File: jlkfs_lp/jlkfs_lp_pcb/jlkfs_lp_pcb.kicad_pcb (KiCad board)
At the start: 2 copper layers, 158.1 x 125.8 mm, 40 parts, among them J0 USB_C_Receptacle_PowerOnly_6P, SW0 SWITCH, SW1 SWITCH, SW10 SWITCH, SW11 SWITCH, SW12 SWITCH, SW13 SWITCH, SW14 SWITCH, SW15 SWITCH, SW16 SWITCH, SW17 SWITCH, SW18 SWITCH, SW19 SWITCH, SW2 SWITCH, SW20 SWITCH, SW21 SWITCH, SW22 SWITCH, SW23 SWITCH, SW24 SWITCH, SW25 SWITCH, SW26 SWITCH, SW27 SWITCH, SW28 SWITCH, SW3 SWITCH, SW4 SWITCH, SW5 SWITCH, SW6 SWITCH, SW7 SWITCH, SW8 SWITCH, SW9 SWITCH, U0 RP2040

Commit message: Updates to jlkfs_lp.
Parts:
- removed H4, H5: MountingHole, MountingHole:MountingHole_3.5mm
- moved H1 134.4 mm to (95.0, 51.8)
- moved H2 117.2 mm to (142.5, 126.5)
- moved H0 68.9 mm to (171.0, 29.5)
- moved H3 54.2 mm to (228.0, 82.9)
- moved SW0 6.79 mm to (114.0, 51.8)
- moved SW12 6.79 mm to (95.0, 90.1)
- moved SW13 6.79 mm to (114.0, 87.8)
- moved SW19 6.79 mm to (95.0, 108.1)
- moved SW20 6.79 mm to (114.0, 105.8)
- moved SW5 6.79 mm to (95.0, 72.1)
- moved SW6 6.79 mm to (114.0, 69.8)
- moved J0 6.79 mm to (190.0, 20.0)
- moved R0 6.79 mm to (206.0, 34.0)
- moved R1 6.79 mm to (205.9, 36.5)
- moved SW1 6.79 mm to (133.0, 42.9)
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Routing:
- net GND: vias 0 -> 6
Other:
- board size 158.1 x 125.8 mm -> 157.5 x 125.8 mm

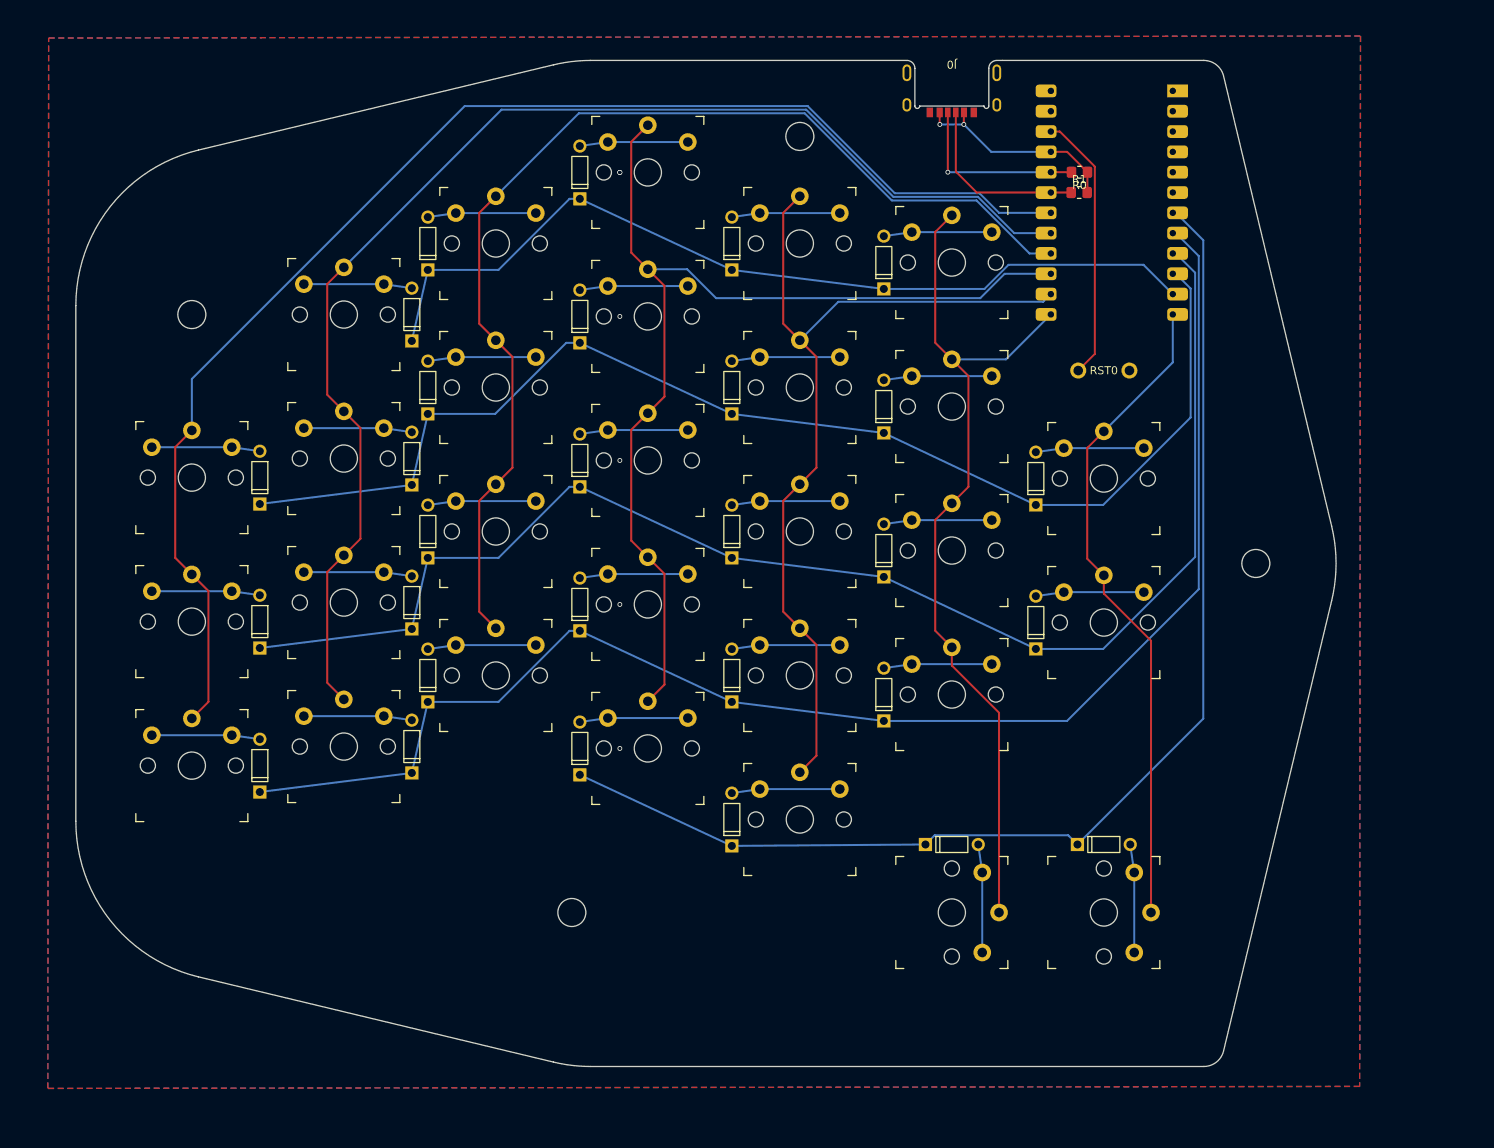
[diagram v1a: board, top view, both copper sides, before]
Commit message: Added a battery path for nice!nano to jlkfs.
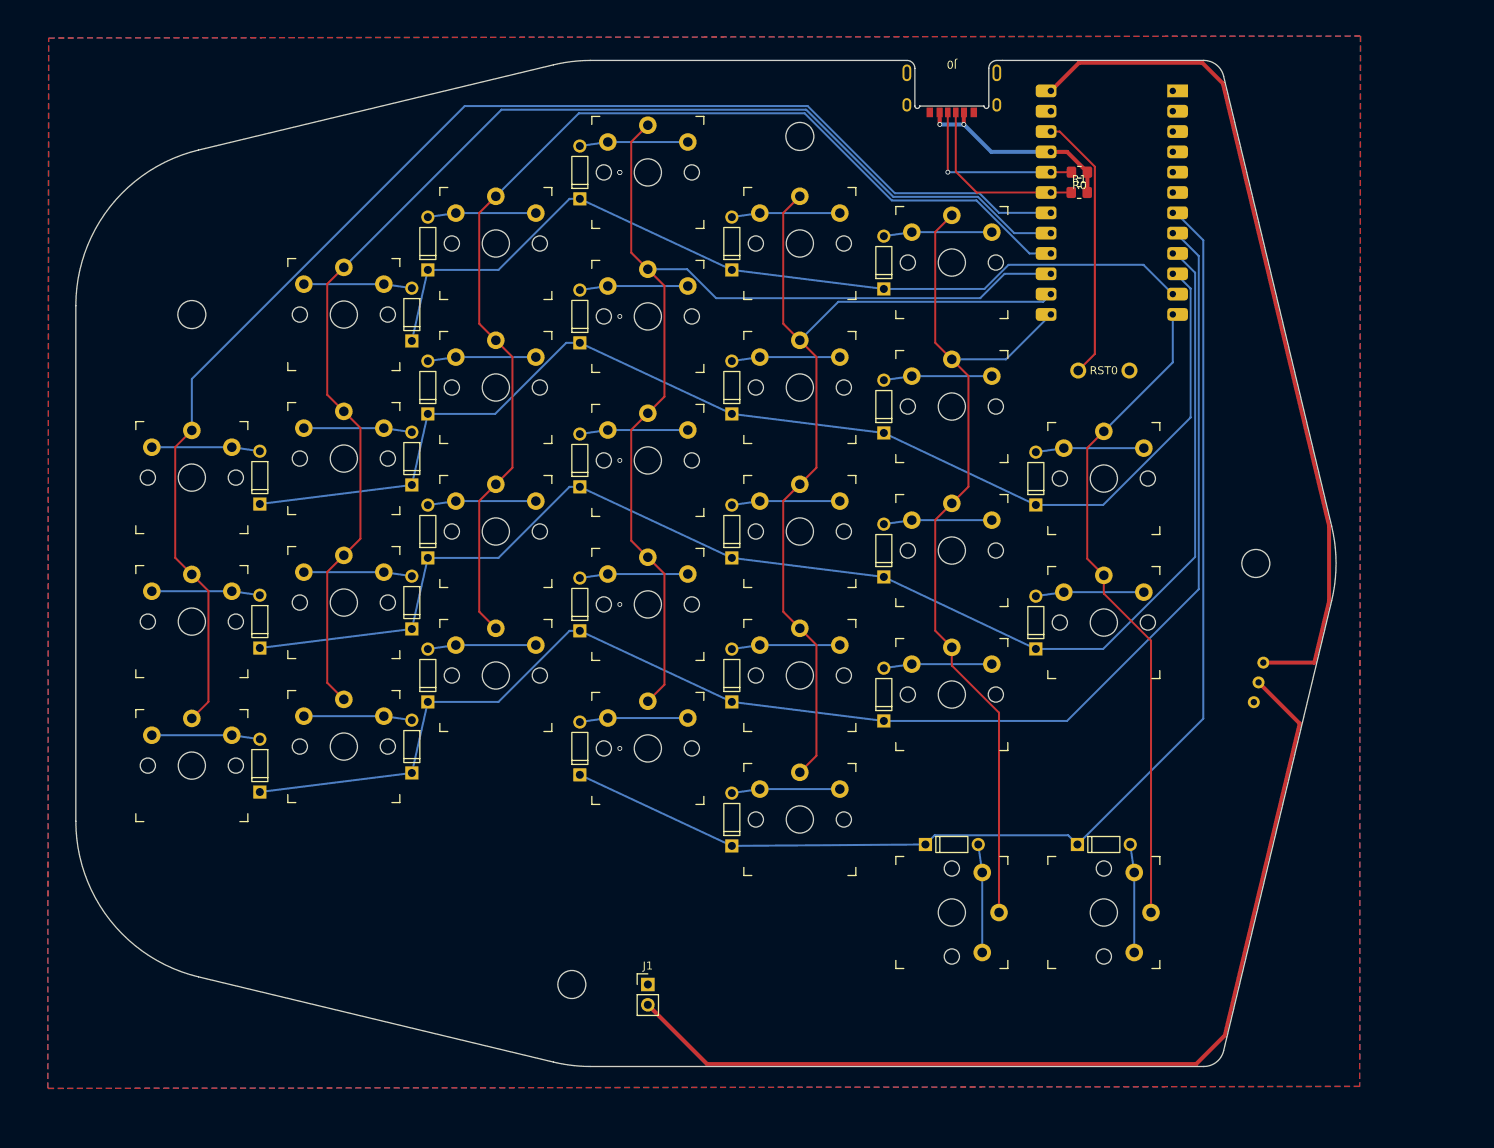
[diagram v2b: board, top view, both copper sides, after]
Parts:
- added J1: Conn_01x02_Socket, Connector_PinHeader_2.54mm:PinHeader_1x02_P2.54mm_Vertical, F.Cu at (152.0, 135.5)
- added PWR0: POWER, footprints:power_switch_1, F.Cu at (234.7, 99.3)
- U0: value RP2040 -> MCU
- moved H2 9.00 mm to (142.5, 135.5)
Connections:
- U0 pad 24: unconnected-(U0-RAW-Pad24) -> /RAW
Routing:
- net /B+: track 0.00 -> 124.0 mm
- net /RAW: track 0.00 -> 104.6 mm
